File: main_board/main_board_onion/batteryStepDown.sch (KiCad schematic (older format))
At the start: 13 parts, among them J13 Power In, J14 Conn_01x02_Female, J15 Conn_01x01_Female, J16 Conn_01x02_Female, U6 LMZM23601V5, U7 lp3965v3

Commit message: Added nRF page and Adafruit Trinket files
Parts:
- removed J13: Power In, Connector_PinHeader_2.54mm:PinHeader_1x02_P2.54mm_Vertical, symbol Connector:Conn_01x02_Female
- removed J14, J16: Conn_01x02_Female, Connector_PinHeader_2.54mm:PinHeader_1x02_P2.54mm_Vertical, symbol Connector:Conn_01x02_Female
- removed J15: Conn_01x01_Female, Connector_PinHeader_2.54mm:PinHeader_1x01_P2.54mm_Vertical, symbol Connector:Conn_01x01_Female
- added D6: Green, LED_SMD:LED_0603_1608Metric, symbol Device:LED
- added D7: Red, LED_SMD:LED_0603_1608Metric, symbol Device:LED
- added R39, R40: 1k, Resistor_SMD:R_0603_1608Metric, symbol Device:R
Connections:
- wire segments 54 -> 57
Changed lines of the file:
@@
 $Descr A4 11693 8268
 encoding utf-8
-Sheet 4 5
+Sheet 4 6
 Title ""
 Date ""
@@
 $EndComp
 $Comp
-L Connector:Conn_01x02_Female J13
-U 1 1 5CB0F652
-P 1125 1850
-F 0 "J13" H 1017 1525 50  0000 C CNN
-F 1 "Power In" H 1017 1616 50  0000 C CNN
-F 2 "Connector_PinHeader_2.54mm:PinHeader_1x02_P2.54mm_Vertical" H 1125 1850 50  0001 C CNN
-F 3 "~" H 1125 1850 50  0001 C CNN
-	1    1125 1850
-	-1   0    0    1
-$EndComp
-Text Label 1375 1850 0    50   ~ 0
-GND_Batt
-Text Label 1375 1750 0    50   ~ 0
-Batt_In
-$Comp
 L Device:C_Small C26
 U 1 1 5CB12BC7
@@
 Connection ~ 6925 2500
 Wire Wire Line
-	6925 2500 7300 2500
+	6925 2500 7525 2500
 Wire Wire Line
 	6925 2700 6925 3025
@@
 	1    0    0    -1
 $EndComp
-Text Label 5575 2500 2    50   ~ 0
+Text Label 5475 2500 2    50   ~ 0
 5V
 Connection ~ 5550 2500
 Wire Wire Line
-	5550 2500 5425 2500
+	5550 2500 5125 2500
 Wire Wire Line
 	5550 2700 5550 2900
@@
 Wire Wire Line
 	1925 3625 1525 3625
-Wire Wire Line
-	1325 1850 1750 1850
-Wire Wire Line
-	1325 1750 1650 1750
 Text Label 2825 2525 2    50   ~ 0
 Batt_In
@@
 Text Label 7150 2500 0    50   ~ 0
 3v3
-$Comp
-L Connector:Conn_01x02_Female J14
-U 1 1 5CB169CC
-P 5025 1775
-F 0 "J14" H 5053 1751 50  0000 L CNN
-F 1 "Conn_01x02_Female" H 5053 1660 50  0000 L CNN
-F 2 "Connector_PinHeader_2.54mm:PinHeader_1x02_P2.54mm_Vertical" H 5025 1775 50  0001 C CNN
-F 3 "~" H 5025 1775 50  0001 C CNN
-	1    5025 1775
-	1    0    0    -1
-$EndComp
-$Comp
-L Connector:Conn_01x02_Female J16
-U 1 1 5CB16ED5
-P 7800 1775
-F 0 "J16" H 7828 1751 50  0000 L CNN
-F 1 "Conn_01x02_Female" H 7828 1660 50  0000 L CNN
-F 2 "Connector_PinHeader_2.54mm:PinHeader_1x02_P2.54mm_Vertical" H 7800 1775 50  0001 C CNN
-F 3 "~" H 7800 1775 50  0001 C CNN
-	1    7800 1775
-	1    0    0    -1
-$EndComp
-Text Label 4750 1775 2    50   ~ 0
-GND
-Text Label 4750 1875 2    50   ~ 0
-5V
-Wire Wire Line
-	4825 1875 4650 1875
-Wire Wire Line
-	4825 1775 4600 1775
-Text Label 7550 1775 2    50   ~ 0
-GND
-Text Label 7550 1875 2    50   ~ 0
-3v3
-Wire Wire Line
-	7600 1875 7400 1875
-Wire Wire Line
-	7600 1775 7375 1775
 Text HLabel 1025 925  0    50   Input ~ 0
 Pack+
@@
 Wire Wire Line
 	2850 2725 2650 2725
-$Comp
-L Connector:Conn_01x01_Female J15
-U 1 1 5CB8B93E
-P 5025 2100
-F 0 "J15" H 5053 2126 50  0000 L CNN
-F 1 "Conn_01x01_Female" H 5053 2035 50  0000 L CNN
-F 2 "Connector_PinHeader_2.54mm:PinHeader_1x01_P2.54mm_Vertical" H 5025 2100 50  0001 C CNN
-F 3 "~" H 5025 2100 50  0001 C CNN
-	1    5025 2100
-	1    0    0    -1
-$EndComp
 Text Label 3900 2925 0    50   ~ 0
 PG
 Wire Wire Line
 	3850 2925 4050 2925
-Text Label 4675 2100 0    50   ~ 0
-PG
-Wire Wire Line
-	4625 2100 4825 2100
 Wire Wire Line
 	3350 3175 4500 3175
@@
 Wire Wire Line
 	5225 3275 5450 3275
+Text HLabel 7800 2500 2    50   Output ~ 0
+3v3
+Text HLabel 4925 2500 0    50   Output ~ 0
+5V
+$Comp
+L Device:R R39
+U 1 1 5D11C709
+P 5125 2250
+F 0 "R39" H 5195 2296 50  0000 L CNN
+F 1 "1k" H 5195 2205 50  0000 L CNN
+F 2 "Resistor_SMD:R_0603_1608Metric" V 5055 2250 50  0001 C CNN
+F 3 "~" H 5125 2250 50  0001 C CNN
+	1    5125 2250
+	1    0    0    -1
+$EndComp
+$Comp
+L Device:LED D6
+U 1 1 5D11C977
+P 5125 1900
+F 0 "D6" V 5072 1978 50  0000 L CNN
+F 1 "Green" V 5163 1978 50  0000 L CNN
+F 2 "LED_SMD:LED_0603_1608Metric" H 5125 1900 50  0001 C CNN
+F 3 "~" H 5125 1900 50  0001 C CNN
+	1    5125 1900
+	0    1    1    0
+$EndComp
+Text Label 5275 1725 2    50   ~ 0
+GND
+Wire Wire Line
+	5125 2400 5125 2500
+Connection ~ 5125 2500
+Wire Wire Line
+	5125 2500 4925 2500
+Wire Wire Line
+	5125 2100 5125 2050
+Wire Wire Line
+	5125 1750 5125 1725
+Wire Wire Line
+	5125 1725 5275 1725
+Text Label 7675 1725 2    50   ~ 0
+GND
+Wire Wire Line
+	7525 1750 7525 1725
+Wire Wire Line
+	7525 2100 7525 2050
+Wire Wire Line
+	7525 1725 7675 1725
+$Comp
+L Device:LED D7
+U 1 1 5D1204D2
+P 7525 1900
+F 0 "D7" V 7472 1978 50  0000 L CNN
+F 1 "Red" V 7563 1978 50  0000 L CNN
+F 2 "LED_SMD:LED_0603_1608Metric" H 7525 1900 50  0001 C CNN
+F 3 "~" H 7525 1900 50  0001 C CNN
+	1    7525 1900
+	0    1    1    0
+$EndComp
+$Comp
+L Device:R R40
+U 1 1 5D1204D3
+P 7525 2250
+F 0 "R40" H 7595 2296 50  0000 L CNN
+F 1 "1k" H 7595 2205 50  0000 L CNN
+F 2 "Resistor_SMD:R_0603_1608Metric" V 7455 2250 50  0001 C CNN
+F 3 "~" H 7525 2250 50  0001 C CNN
+	1    7525 2250
+	1    0    0    -1
+$EndComp
+Wire Wire Line
+	7525 2400 7525 2500
+Connection ~ 7525 2500
+Wire Wire Line
+	7525 2500 7800 2500
 $EndSCHEMATC

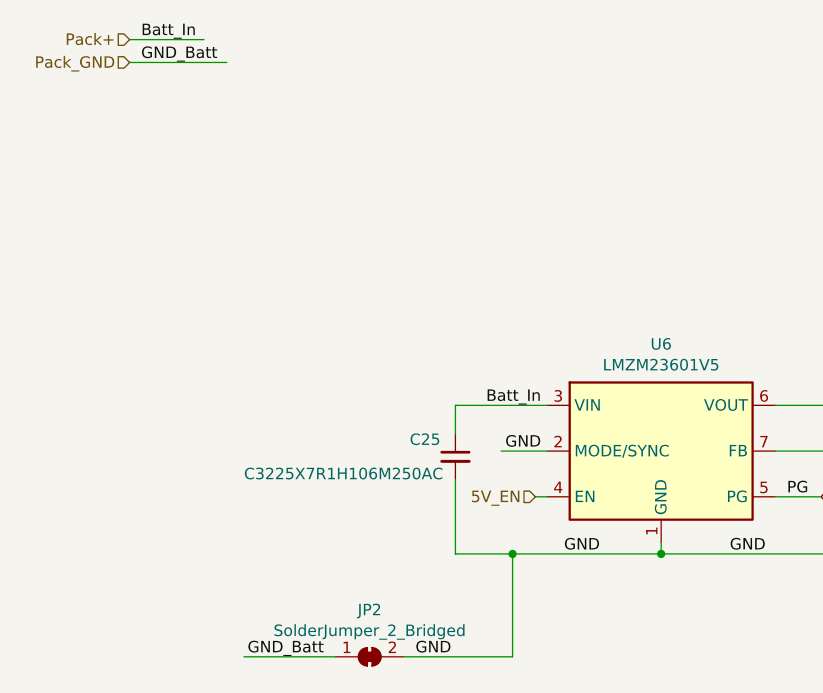
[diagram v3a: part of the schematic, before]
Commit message: Finished initial routing of this design
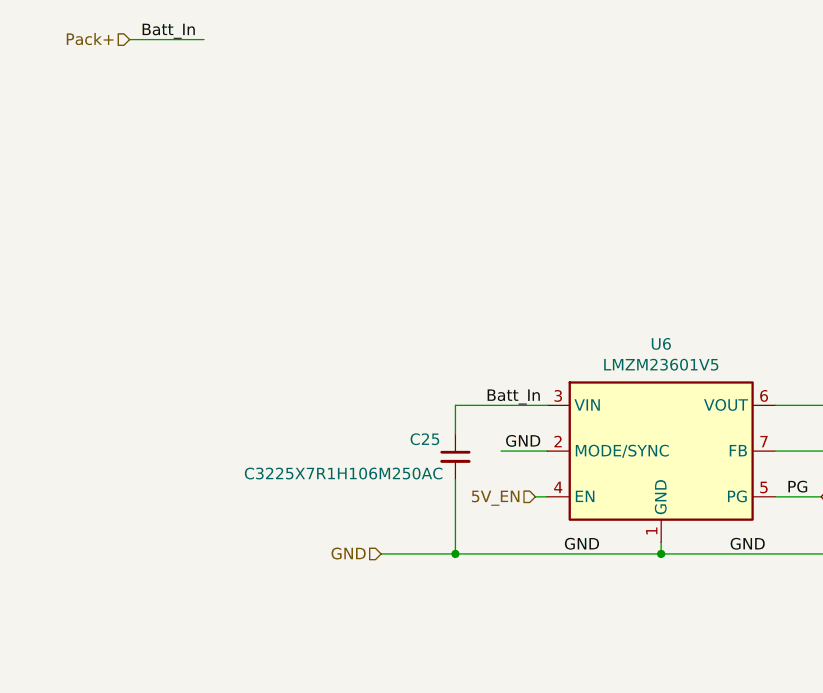
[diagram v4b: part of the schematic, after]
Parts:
- removed JP2: SolderJumper_2_Bridged, Jumper:SolderJumper-2_P1.3mm_Bridged_Pad1.0x1.5mm, symbol Jumper:SolderJumper_2_Bridged
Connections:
- net labels removed: GND_Batt, Pack_GND
- wire segments 57 -> 53
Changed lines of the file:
@@
 $Descr A4 11693 8268
 encoding utf-8
-Sheet 4 7
+Sheet 3 7
 Title ""
 Date ""
@@
 Text Label 6575 3025 0    50   ~ 0
 GND
-$Comp
-L Jumper:SolderJumper_2_Bridged JP2
-U 1 1 5CB412D6
-P 2075 3625
-F 0 "JP2" H 2075 3830 50  0000 C CNN
-F 1 "SolderJumper_2_Bridged" H 2075 3739 50  0000 C CNN
-F 2 "Jumper:SolderJumper-2_P1.3mm_Bridged_Pad1.0x1.5mm" H 2075 3625 50  0001 C CNN
-F 3 "~" H 2075 3625 50  0001 C CNN
-	1    2075 3625
-	1    0    0    -1
-$EndComp
-Text Label 1875 3625 2    50   ~ 0
-GND_Batt
-Text Label 2275 3625 0    50   ~ 0
-GND
-Wire Wire Line
-	1925 3625 1525 3625
 Text Label 2825 2525 2    50   ~ 0
 Batt_In
@@
 Text HLabel 1025 925  0    50   Input ~ 0
 Pack+
-Text HLabel 1025 1025 0    50   Input ~ 0
-Pack_GND
-Text Label 1075 1025 0    50   ~ 0
-GND_Batt
 Text Label 1075 925  0    50   ~ 0
 Batt_In
 Wire Wire Line
-	1025 1025 1450 1025
-Wire Wire Line
 	1025 925  1350 925
-Wire Wire Line
-	2450 3175 2700 3175
 Text Label 2825 2725 2    50   ~ 0
 GND
@@
 Text Label 2925 3175 0    50   ~ 0
 GND
-Wire Wire Line
-	2700 3625 2700 3175
-Wire Wire Line
-	2225 3625 2700 3625
-Connection ~ 2700 3175
-Wire Wire Line
-	2700 3175 3350 3175
 Wire Wire Line
 	4500 3175 5550 3175
@@
 	1    0    0    -1
 $EndComp
+Wire Wire Line
+	2450 3175 3350 3175
+Text HLabel 2125 3175 0    50   Input ~ 0
+GND
+Wire Wire Line
+	2450 3175 2125 3175
+Connection ~ 2450 3175
 $EndSCHEMATC

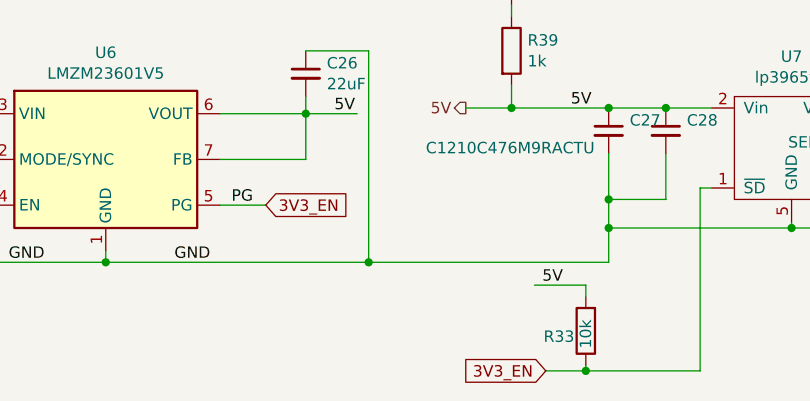
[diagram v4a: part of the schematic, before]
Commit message: went back to original Macrofab v2 files and made changes for v3.5
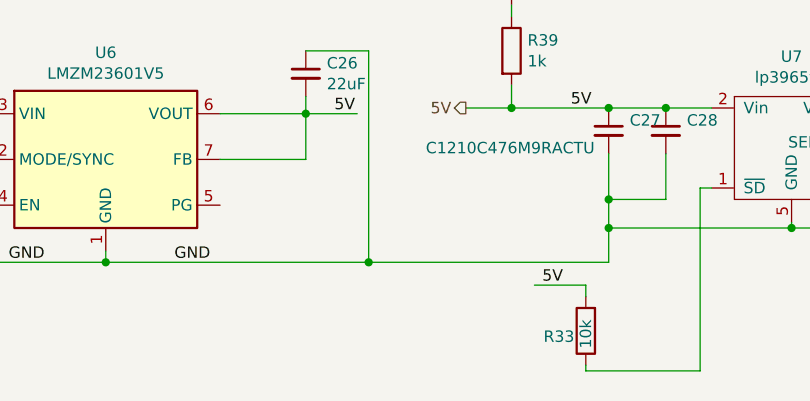
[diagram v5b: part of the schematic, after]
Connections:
- net labels removed: 3V3_EN, PG
- wire segments 53 -> 51
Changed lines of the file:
@@
-EESchema Schematic File Version 5
+EESchema Schematic File Version 4
 LIBS:main_board_onion-cache
-EELAYER 29 0
+EELAYER 30 0
 EELAYER END
 $Descr A4 11693 8268
@@
 Wire Wire Line
 	2850 2725 2650 2725
-Text Label 3900 2925 0    50   ~ 0
-PG
-Wire Wire Line
-	3850 2925 4050 2925
 Wire Wire Line
 	3350 3175 4500 3175
@@
 Wire Wire Line
 	2450 2525 2850 2525
-Text GLabel 4050 2925 2    50   Input ~ 0
-3V3_EN
-Text GLabel 5275 3650 0    50   Input ~ 0
-3V3_EN
 Wire Wire Line
 	5800 2500 6000 2500
@@
 $EndComp
 Wire Wire Line
-	5275 3650 5450 3650
-Wire Wire Line
 	5950 2850 5950 3650
 Wire Wire Line
 	5450 3625 5450 3650
-Connection ~ 5450 3650
 Wire Wire Line
 	5450 3650 5950 3650
